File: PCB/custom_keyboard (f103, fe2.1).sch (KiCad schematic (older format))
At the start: 509 parts, among them J1 Conn_01x04, U1 SD00HA, U10 PRTR5V0U2X, U11 MIC2505, U12 XC6206P332MR, U13 74LVC1G34, U2 PRTR5V0U2X, U3 PRTR5V0U2X, U4 PRTR5V0U2X, U5 24LC04BT-I/SN, U6 PRTR5V0U2X, U7 PRTR5V0U2X, U8 PRTR5V0U2X, U9 MIC2505, Y1 12MHz, Y2 8MHz

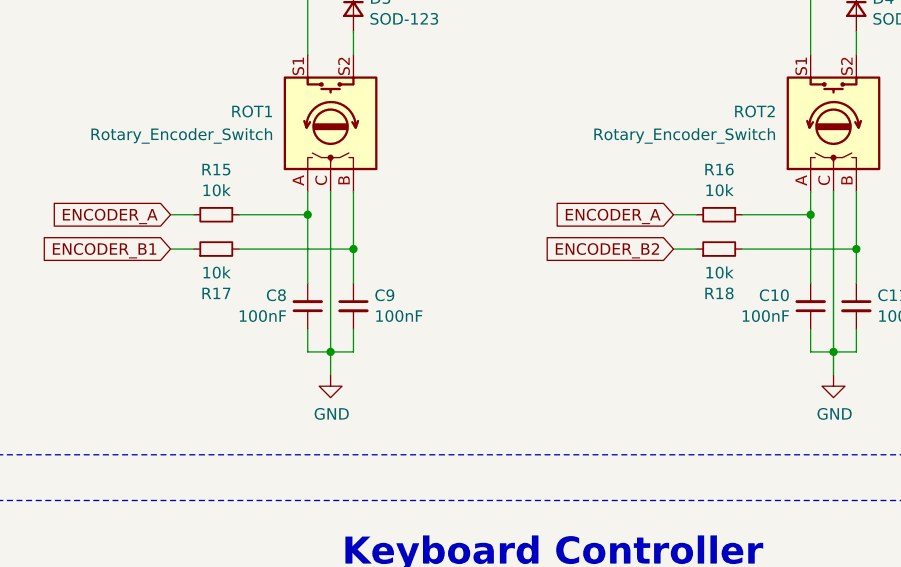
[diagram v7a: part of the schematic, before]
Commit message: Double checked traces
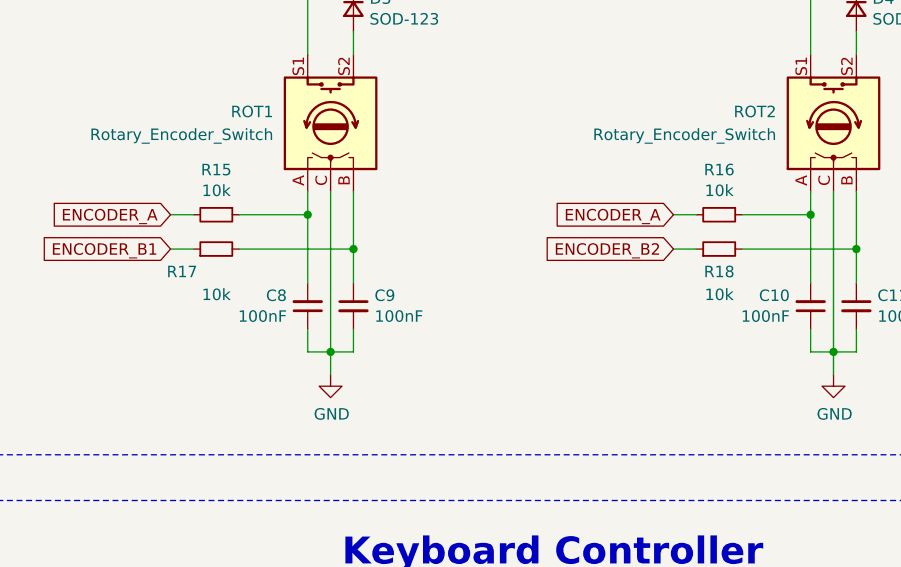
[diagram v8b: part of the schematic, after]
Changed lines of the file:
@@
 U 1 1 75491AA1
 P 7150 13550
-F 0 "R18" V 6954 13550 50  0000 C CNN
-F 1 "10k" V 7045 13550 50  0000 C CNN
+F 0 "R18" V 7050 13550 50  0000 C CNN
+F 1 "10k" V 6950 13550 50  0000 C CNN
 F 2 "Resistor_SMD:R_0805_2012Metric" H 7150 13550 50  0001 C CNN
 F 3 "~" H 7150 13550 50  0001 C CNN
@@
 	5450 13300 5450 14000
 $Comp
-L Device:R_Small R17
-U 1 1 851C8659
-P 4950 13550
-F 0 "R17" V 4754 13550 50  0000 C CNN
-F 1 "10k" V 4845 13550 50  0000 C CNN
-F 2 "Resistor_SMD:R_0805_2012Metric" H 4950 13550 50  0001 C CNN
-F 3 "~" H 4950 13550 50  0001 C CNN
-F 4 "C17414" H 4950 13550 50  0001 C CNN "LCSC Part"
-	1    4950 13550
-	0    -1   -1   0
-$EndComp
-$Comp
 L Device:R_Small R15
 U 1 1 851C8645
@@
 Connection ~ 14650 12450
 $Comp
-L Connector:TestPoint_Small TP20
-U 1 1 93D39E5C
-P 6900 17450
-F 0 "TP20" H 6850 17500 50  0000 L CNN
-F 1 "TestPoint_Small" H 6948 17405 50  0001 L CNN
-F 2 "TestPoint:TestPoint_THTPad_D1.0mm_Drill0.5mm" H 7100 17450 50  0001 C CNN
-F 3 "~" H 7100 17450 50  0001 C CNN
-F 4 "0" H 6900 17450 50  0001 C CNN "JLCPCB BOM"
-	1    6900 17450
-	-1   0    0    -1
-$EndComp
-$Comp
 L Connector:TestPoint_Small TP51
 U 1 1 93D3A1D0
@@
 $EndComp
 $Comp
-L Connector:TestPoint_Small TP22
-U 1 1 A7E4F619
-P 6800 17550
-F 0 "TP22" H 6700 17600 50  0000 L CNN
-F 1 "TestPoint_Small" H 6848 17505 50  0001 L CNN
-F 2 "TestPoint:TestPoint_THTPad_D1.0mm_Drill0.5mm" H 7000 17550 50  0001 C CNN
-F 3 "~" H 7000 17550 50  0001 C CNN
-F 4 "0" H 6800 17550 50  0001 C CNN "JLCPCB BOM"
-	1    6800 17550
-	1    0    0    -1
-$EndComp
-$Comp
-L Connector:TestPoint_Small TP24
-U 1 1 A85DD069
-P 6900 17650
-F 0 "TP24" H 6800 17700 50  0000 L CNN
-F 1 "TestPoint_Small" H 6948 17605 50  0001 L CNN
-F 2 "TestPoint:TestPoint_THTPad_D1.0mm_Drill0.5mm" H 7100 17650 50  0001 C CNN
-F 3 "~" H 7100 17650 50  0001 C CNN
-F 4 "0" H 6900 17650 50  0001 C CNN "JLCPCB BOM"
-	1    6900 17650
-	1    0    0    -1
-$EndComp
-$Comp
-L Connector:TestPoint_Small TP28
-U 1 1 A85DD345
-P 6900 17850
-F 0 "TP28" H 6800 17900 50  0000 L CNN
-F 1 "TestPoint_Small" H 6948 17805 50  0001 L CNN
-F 2 "TestPoint:TestPoint_THTPad_D1.0mm_Drill0.5mm" H 7100 17850 50  0001 C CNN
-F 3 "~" H 7100 17850 50  0001 C CNN
-F 4 "0" H 6900 17850 50  0001 C CNN "JLCPCB BOM"
-	1    6900 17850
-	1    0    0    -1
-$EndComp
-$Comp
 L Connector:TestPoint_Small TP34
 U 1 1 A85DD541
@@
 	1    0    0    -1
 $EndComp
-$Comp
-L Connector:TestPoint_Small TP26
-U 1 1 A85E2F3B
-P 6800 17750
-F 0 "TP26" H 6700 17800 50  0000 L CNN
-F 1 "TestPoint_Small" H 6848 17705 50  0001 L CNN
-F 2 "TestPoint:TestPoint_THTPad_D1.0mm_Drill0.5mm" H 7000 17750 50  0001 C CNN
-F 3 "~" H 7000 17750 50  0001 C CNN
-F 4 "0" H 6800 17750 50  0001 C CNN "JLCPCB BOM"
-	1    6800 17750
-	1    0    0    -1
-$EndComp
 Wire Wire Line
 	14000 13150 14000 13350
@@
 Wire Wire Line
 	5100 17650 5350 17650
-$Comp
-L Connector:TestPoint_Small TP13
-U 1 1 B1C43BCE
-P 5100 16550
-F 0 "TP13" H 5000 16600 50  0000 L CNN
-F 1 "TestPoint_Small" H 5148 16505 50  0001 L CNN
-F 2 "TestPoint:TestPoint_THTPad_D1.0mm_Drill0.5mm" H 5300 16550 50  0001 C CNN
-F 3 "~" H 5300 16550 50  0001 C CNN
-F 4 "0" H 5100 16550 50  0001 C CNN "JLCPCB BOM"
-	1    5100 16550
-	1    0    0    -1
-$EndComp
 Connection ~ 5100 16550
 Wire Wire Line
@@
 Wire Wire Line
 	23550 16250 23650 16250
+$Comp
+L Connector:TestPoint_Small TP28
+U 1 1 A85DD345
+P 6900 17850
+F 0 "TP28" H 6800 17900 50  0000 L CNN
+F 1 "TestPoint_Small" H 6948 17805 50  0001 L CNN
+F 2 "TestPoint:TestPoint_THTPad_D1.0mm_Drill0.5mm" H 7100 17850 50  0001 C CNN
+F 3 "~" H 7100 17850 50  0001 C CNN
+F 4 "0" H 6900 17850 50  0001 C CNN "JLCPCB BOM"
+	1    6900 17850
+	1    0    0    -1
+$EndComp
+$Comp
+L Connector:TestPoint_Small TP26
+U 1 1 A85E2F3B
+P 6800 17750
+F 0 "TP26" H 6700 17800 50  0000 L CNN
+F 1 "TestPoint_Small" H 6848 17705 50  0001 L CNN
+F 2 "TestPoint:TestPoint_THTPad_D1.0mm_Drill0.5mm" H 7000 17750 50  0001 C CNN
+F 3 "~" H 7000 17750 50  0001 C CNN
+F 4 "0" H 6800 17750 50  0001 C CNN "JLCPCB BOM"
+	1    6800 17750
+	1    0    0    -1
+$EndComp
+$Comp
+L Connector:TestPoint_Small TP24
+U 1 1 A85DD069
+P 6900 17650
+F 0 "TP24" H 6800 17700 50  0000 L CNN
+F 1 "TestPoint_Small" H 6948 17605 50  0001 L CNN
+F 2 "TestPoint:TestPoint_THTPad_D1.0mm_Drill0.5mm" H 7100 17650 50  0001 C CNN
+F 3 "~" H 7100 17650 50  0001 C CNN
+F 4 "0" H 6900 17650 50  0001 C CNN "JLCPCB BOM"
+	1    6900 17650
+	1    0    0    -1
+$EndComp
+$Comp
+L Connector:TestPoint_Small TP22
+U 1 1 A7E4F619
+P 6800 17550
+F 0 "TP22" H 6700 17600 50  0000 L CNN
+F 1 "TestPoint_Small" H 6848 17505 50  0001 L CNN
+F 2 "TestPoint:TestPoint_THTPad_D1.0mm_Drill0.5mm" H 7000 17550 50  0001 C CNN
+F 3 "~" H 7000 17550 50  0001 C CNN
+F 4 "0" H 6800 17550 50  0001 C CNN "JLCPCB BOM"
+	1    6800 17550
+	1    0    0    -1
+$EndComp
+$Comp
+L Connector:TestPoint_Small TP20
+U 1 1 93D39E5C
+P 6900 17450
+F 0 "TP20" H 6850 17500 50  0000 L CNN
+F 1 "TestPoint_Small" H 6948 17405 50  0001 L CNN
+F 2 "TestPoint:TestPoint_THTPad_D1.0mm_Drill0.5mm" H 7100 17450 50  0001 C CNN
+F 3 "~" H 7100 17450 50  0001 C CNN
+F 4 "0" H 6900 17450 50  0001 C CNN "JLCPCB BOM"
+	1    6900 17450
+	-1   0    0    -1
+$EndComp
+$Comp
+L Connector:TestPoint_Small TP13
+U 1 1 B1C43BCE
+P 5100 16550
+F 0 "TP13" H 5000 16600 50  0000 L CNN
+F 1 "TestPoint_Small" H 5148 16505 50  0001 L CNN
+F 2 "TestPoint:TestPoint_THTPad_D1.0mm_Drill0.5mm" H 5300 16550 50  0001 C CNN
+F 3 "~" H 5300 16550 50  0001 C CNN
+F 4 "0" H 5100 16550 50  0001 C CNN "JLCPCB BOM"
+	1    5100 16550
+	1    0    0    -1
+$EndComp
+$Comp
+L Device:R_Small R17
+U 1 1 851C8659
+P 4950 13550
+F 0 "R17" V 4850 13700 50  0000 C CNN
+F 1 "10k" V 4750 13550 50  0000 C CNN
+F 2 "Resistor_SMD:R_0805_2012Metric" H 4950 13550 50  0001 C CNN
+F 3 "~" H 4950 13550 50  0001 C CNN
+F 4 "C17414" H 4950 13550 50  0001 C CNN "LCSC Part"
+	1    4950 13550
+	0    -1   -1   0
+$EndComp
 $EndSCHEMATC
